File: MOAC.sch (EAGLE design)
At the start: 57 parts, among them IC1 ATMEGA32U4-QFN

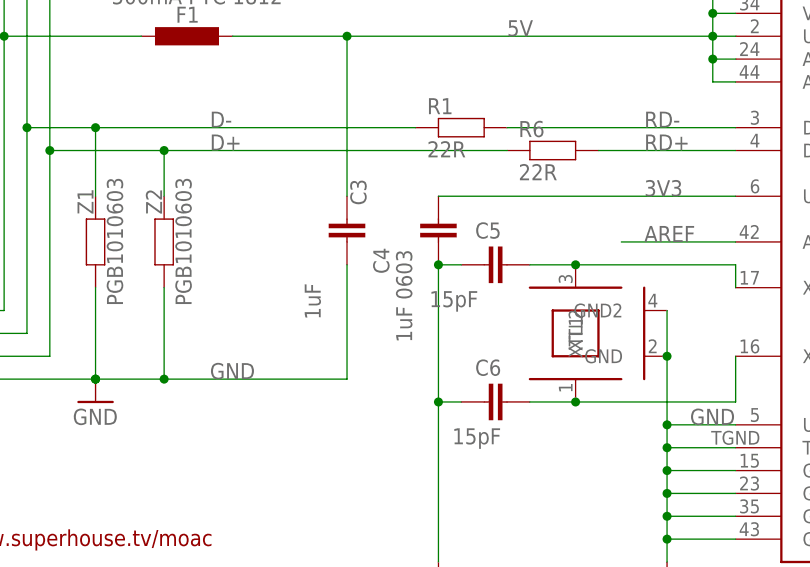
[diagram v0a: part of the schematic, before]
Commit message: Improved designators
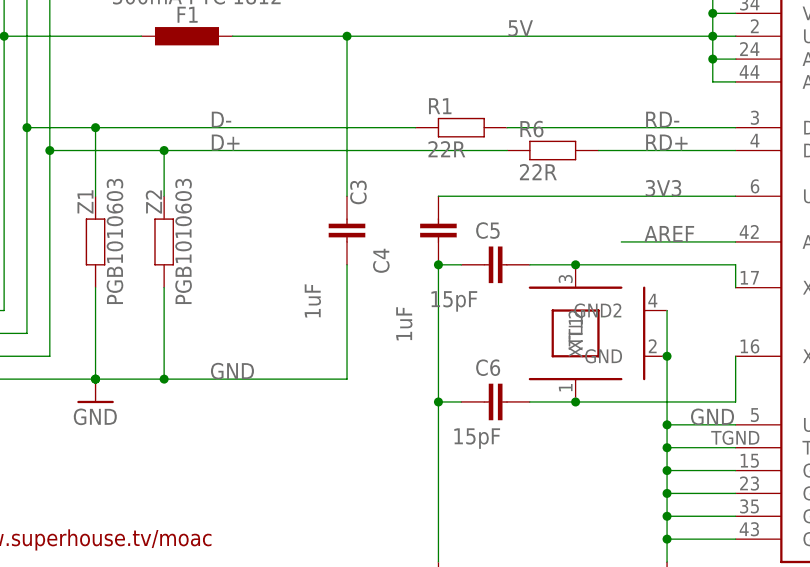
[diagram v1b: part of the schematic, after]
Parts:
- C4: value 1uF 0603 -> 1uF
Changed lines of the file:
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@@
 <part name="C6" library="freetronics-master-v1.1" deviceset="CAP" device="0603" value="15pF"/>
 <part name="GND16" library="SparkFun" deviceset="GND" device=""/>
-<part name="C4" library="freetronics-master-v1.1" deviceset="CAP" device="0603" value="1uF 0603"/>
+<part name="C4" library="freetronics-master-v1.1" deviceset="CAP" device="0603" value="1uF"/>
 <part name="GND5" library="SparkFun" deviceset="GND" device=""/>
 <part name="XTL1" library="freetronics-jon" deviceset="CRYSTAL-GND" device="3X2" value="16MHz"/>

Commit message: Replaced parts using SuperHouse libraries to add 3D models
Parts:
- removed JP2: OLED, freetronics-jon:M04PTH
- removed S1, S2, S3, S4, S5, S6, S7, S8: 3.5mm, freetronics-jon:AUDIO-JACK-PJ321
- removed S21: RESET, freetronics-jon:TAC_SWITCH_2PINSMT
- removed S22: HWB, freetronics-jon:TAC_SWITCH_2PINSMT
- removed U$15: USB-C, freetronics-jon:USB-C
- added J1, J2, J3, J4, J5, J6, J7, J8: 3.5mm, SuperHouse-Connectors:AUDIO-JACK-PJ321
- added J9: USB-C, SuperHouse-Connectors:USB-C
- added MOD1: OLED-I2C128X32-0.91, SuperHouse-Displays:OLED-I2C128X32-0.91
- added S10: HWB, SuperHouse-Switches:TAC_SWITCH_2PINSMT
- added S9: RESET, SuperHouse-Switches:TAC_SWITCH_2PINSMT
- C1, C2, C3, C4, C5, C6: device freetronics-master-v1.1:CAP0603 -> SuperHouse-DiscreteSemi:CAP0603
- F1: device rcl:L-EUL1812 -> SuperHouse-Fuses:PTC050
- ICSP: device pinhead:PINHD-2X3 -> SuperHouse-Connectors:ICSPPTH
- JP1: device freetronics-jon:M02PTH -> SuperHouse-Connectors:M02-PLAIN
- LED1, LED2, LED3, LED4: device freetronics-jon:LED0603 -> SuperHouse-LEDs:LED0603
- PIEZO: device freetronics-master-v1:BUZZERSMD12X12 -> SuperHouse-Audio:BUZZERSMD12X12
- R1, R10, R11, R12, R13, R14, R15, R16, R17, R19, R20, R21, R22, R23, R24, R25, R3, R4, R5, R6, R8, R9: device freetronics-jon:RESISTOR0603 -> SuperHouse-DiscreteSemi:RESISTOR0603
- R18, R7: device freetronics-original:RESISTOR0603 -> SuperHouse-DiscreteSemi:RESISTOR0603
- R2: device freetronics-master-v1.1:RESISTOR0603 -> SuperHouse-DiscreteSemi:RESISTOR0603
- XTL1: device freetronics-jon:CRYSTAL-GND3X2 -> SuperHouse-Oscillators:CRYSTAL-GND3X2
- Z1, Z2: device freetronics-master-v1.1:RESISTOR0603 -> SuperHouse-DiscreteSemi:TVS0603
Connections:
- net 5V: now also MOD1.VCC; no longer JP2.3
- net D+: now also J9.D+@A6, J9.D+@B6; no longer U$15.D+@A6, U$15.D+@B6
- net D-: now also J9.D-@A7, J9.D-@B7; no longer U$15.D-@A7, U$15.D-@B7
- net D2_SDA: now also MOD1.SDA; no longer JP2.1
- net D3_SCL: now also MOD1.SCL; no longer JP2.2
- net GND: now also J1.3, J2.3, J3.3, J4.3, J5.3, J6.3, J7.3, J8.3, J9.GND@A1, J9.GND@A12, J9.GND@B1, J9.GND@B12, J9.GND@CASE1, J9.GND@CASE2, J9.GND@CASE3, J9.GND@CASE4, J9.GND@FIX1, J9.GND@FIX2, J9.GND@FIX3, J9.GND@FIX4, MOD1.GND, S10.S, S9.P; no longer JP2.4, S1.3, S2.3, S21.P, S22.S, S3.3, S4.3, S5.3, S6.3, S7.3, S8.3, U$15.GND@A1, U$15.GND@A12, U$15.GND@B1, U$15.GND@B12, U$15.GND@CASE1, U$15.GND@CASE2, U$15.GND@CASE3, U$15.GND@CASE4, U$15.GND@FIX1, U$15.GND@FIX2, U$15.GND@FIX3, U$15.GND@FIX4
- net HWB: now also S10.P; no longer S22.P
- net N$1: now also J9.CC2; no longer U$15.CC2
- net N$10: now also J5.4A, J5.4B; no longer S5.4A, S5.4B
- net N$13: now also J6.4A, J6.4B; no longer S6.4A, S6.4B
- net N$14: now also J7.4A, J7.4B; no longer S7.4A, S7.4B
- net N$15: now also J8.4A, J8.4B; no longer S8.4A, S8.4B
- net N$3: now also J1.4A, J1.4B; no longer S1.4A, S1.4B
- net N$4: now also J2.4A, J2.4B; no longer S2.4A, S2.4B
- net N$5: now also J3.4A, J3.4B; no longer S3.4A, S3.4B
- net N$67: now also J9.CC1; no longer U$15.CC1
- net N$9: now also J4.4A, J4.4B; no longer S4.4A, S4.4B
- net RESET: now also S9.S; no longer S21.S
- net USB+: now also J9.V+@A4, J9.V+@A9, J9.V+@B4, J9.V+@B9; no longer U$15.V+@A4, U$15.V+@A9, U$15.V+@B4, U$15.V+@B9
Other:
- note added: "(C)2019 SuperHouse Automation Pty Ltd: www.superhouse.tv"
- note added: "V1.1 (2019-07-07)"
- note removed: "(C)2018 SuperHouse Automation Pty Ltd: www.superhouse.tv"
- note removed: "V1.0 (2018-10-10)"

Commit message: Replaced 128x32 OLED with 128x64, 1.3in for v2.0 release
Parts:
- removed MOD1: OLED-I2C128X32-0.91, SuperHouse-Displays:OLED-I2C128X32-0.91
- added MOD2: OLED-I2C128X64-1.3-HO, SuperHouse-Displays:OLED-I2C128X64-1.3-HO
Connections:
- net 5V: now also MOD2.VCC; no longer MOD1.VCC
- net D2_SDA: now also MOD2.SDA; no longer MOD1.SDA
- net D3_SCL: now also MOD2.SCL; no longer MOD1.SCL
- net GND: now also MOD2.GND; no longer MOD1.GND
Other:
- note added: "(C)2018-2019 SuperHouse Automation Pty Ltd: www.superhouse.tv"
- note added: "128x64 OLED Module"
- note added: "V2.0 (2019-07-11)"
- note removed: "(C)2019 SuperHouse Automation Pty Ltd: www.superhouse.tv"
- note removed: "128x32 OLED Header"
- note removed: "V1.1 (2019-07-07)"
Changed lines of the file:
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@@
 <part name="U$16" library="SparkFun" deviceset="5V" device=""/>
 <part name="JP1" library="SuperHouse-Connectors" library_urn="urn:adsk.eagle:library:11765989" deviceset="M02" device="-PLAIN" package3d_urn="urn:adsk.eagle:package:11818419/1" value="5V"/>
-<part name="MOD1" library="SuperHouse-Displays" library_urn="urn:adsk.eagle:library:11966779" deviceset="OLED-I2C" device="128X32-0.91" package3d_urn="urn:adsk.eagle:package:11973684/2"/>
+<part name="MOD2" library="SuperHouse-Displays" library_urn="urn:adsk.eagle:library:11966779" deviceset="OLED-I2C" device="128X64-1.3-HO" package3d_urn="urn:adsk.eagle:package:12058301/2" value="OLED-I2C128X64-1.3-HO"/>
 </parts>
 <sheets>
@@
 bootloader with the jumper.</text>
 <text x="7.62" y="20.32" size="3.048" layer="94">Mini Open Adaptive Controller</text>
-<text x="38.1" y="14.478" size="1.778" layer="94">V1.1 (2019-07-07)</text>
+<text x="38.1" y="14.478" size="1.778" layer="94">V2.0 (2019-07-11)</text>
 <text x="7.62" y="14.478" size="1.778" layer="94">SKU: MOAC</text>
-<text x="7.366" y="9.398" size="1.778" layer="94">(C)2019 SuperHouse Automation Pty Ltd: www.superhouse.tv</text>
+<text x="7.366" y="9.398" size="1.778" layer="94">(C)2018-2019 SuperHouse Automation Pty Ltd: www.superhouse.tv</text>
 <text x="7.366" y="6.35" size="1.778" layer="94">Licensed under the TAPR Open Hardware License: www.tapr.org/ohl</text>
 <text x="68.326" y="14.478" size="1.778" layer="94">www.superhouse.tv/moac</text>
@@
 <wire x1="109.22" y1="124.46" x2="109.22" y2="101.6" width="0.4064" layer="97" style="longdash"/>
 <text x="218.44" y="81.28" size="1.778" layer="97">Button3</text>
-<text x="111.76" y="149.86" size="2.54" layer="94" ratio="12">128x32 OLED Header</text>
+<text x="111.76" y="149.86" size="2.54" layer="94" ratio="12">128x64 OLED Module</text>
 <wire x1="109.22" y1="154.94" x2="154.94" y2="154.94" width="0.4064" layer="97" style="longdash"/>
 <wire x1="109.22" y1="124.46" x2="154.94" y2="124.46" width="0.4064" layer="97" style="longdash"/>
@@
 <attribute name="NAME" x="193.04" y="151.638" size="1.778" layer="95" rot="R180"/>
 </instance>
-<instance part="MOD1" gate="G$1" x="134.62" y="137.16" smashed="yes">
-<attribute name="NAME" x="129.54" y="142.748" size="1.778" layer="95"/>
+<instance part="MOD2" gate="G$1" x="132.08" y="137.16" smashed="yes">
+<attribute name="NAME" x="127" y="142.748" size="1.778" layer="95"/>
 <attribute name="VALUE" x="119.38" y="129.54" size="1.778" layer="96"/>
 </instance>
@@
 </segment>
 <segment>
-<pinref part="MOD1" gate="G$1" pin="VCC"/>
-<wire x1="144.78" y1="139.7" x2="149.86" y2="139.7" width="0.1524" layer="91"/>
+<wire x1="142.24" y1="139.7" x2="149.86" y2="139.7" width="0.1524" layer="91"/>
 <pinref part="U$2" gate="G$1" pin="5V"/>
 <wire x1="149.86" y1="139.7" x2="149.86" y2="142.24" width="0.1524" layer="91"/>
+<pinref part="MOD2" gate="G$1" pin="VCC"/>
 </segment>
 </net>
@@
 </segment>
 <segment>
-<pinref part="MOD1" gate="G$1" pin="GND"/>
 <pinref part="GND6" gate="1" pin="GND"/>
-<wire x1="144.78" y1="134.62" x2="149.86" y2="134.62" width="0.1524" layer="91"/>
+<wire x1="142.24" y1="134.62" x2="149.86" y2="134.62" width="0.1524" layer="91"/>
 <wire x1="149.86" y1="134.62" x2="149.86" y2="132.08" width="0.1524" layer="91"/>
+<pinref part="MOD2" gate="G$1" pin="GND"/>
 </segment>
 </net>
@@
 </segment>
 <segment>
-<wire x1="124.46" y1="139.7" x2="119.38" y2="139.7" width="0.1524" layer="91"/>
-<pinref part="MOD1" gate="G$1" pin="SDA"/>
+<wire x1="121.92" y1="139.7" x2="119.38" y2="139.7" width="0.1524" layer="91"/>
 <label x="119.38" y="139.7" size="1.27" layer="95" rot="R180" xref="yes"/>
+<pinref part="MOD2" gate="G$1" pin="SDA"/>
 </segment>
 </net>
@@
 </segment>
 <segment>
-<wire x1="124.46" y1="134.62" x2="119.38" y2="134.62" width="0.1524" layer="91"/>
-<pinref part="MOD1" gate="G$1" pin="SCL"/>
+<wire x1="121.92" y1="134.62" x2="119.38" y2="134.62" width="0.1524" layer="91"/>
 <label x="119.38" y="134.62" size="1.27" layer="95" rot="R180" xref="yes"/>
-</segment>
-</net>
+<pinref part="MOD2" gate="G$1" pin="SCL"/>
+</segment>
+</net>

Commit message: Changed ATmega32U4 from QFN to TQFP to save Jon's sanity for v2.0 release
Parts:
- removed JP1: 5V, SuperHouse-Connectors:M02-PLAIN
- IC1: value ATMEGA32U4-QFN -> ATMEGA32U4NT-TQFP; device freetronics-jon:ATMEGA32U4-QFN -> SuperHouse-MCUs:ATMEGA32U4NT-TQFP
- SJ1: device freetronics-jon:SJN -> SuperHouse-Jumpers:SJ-NORMAL
- SJ2: device freetronics-jon:SJCN -> SuperHouse-Jumpers:SJC-NORMAL
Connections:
- net 5V: no longer JP1.1
- net GND: no longer IC1.TGND, JP1.2

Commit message: Changed button 8 from A11 to A7, to fix Jon's silly mistake from way back in v1.0
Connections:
- net D10_A11 renamed D10_A10
- net D8_A9 renamed D8_A8
- net D9_A10 renamed D9_A9
- removed net D12_A7: IC1.PD6(T1/OC4D/ADC9), R21.2, R25.1
- removed net D6_A8: IC1.PD7(OC4D/ADC10/T0)
- new net D12_A11: IC1.PD6(T1/OC4D/ADC9)
- new net D6_A7: IC1.PD7(OC4D/ADC10/T0), R21.2, R25.1
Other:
- note added: "V2.1 (2019-07-31)"
- note removed: "V2.0 (2019-07-11)"
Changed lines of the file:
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@@
 <part name="U$16" library="SuperHouse-SupplySymbols" library_urn="urn:adsk.eagle:library:11790503" deviceset="5V" device=""/>
 <part name="MOD2" library="SuperHouse-Displays" library_urn="urn:adsk.eagle:library:11966779" deviceset="OLED-I2C" device="128X64-1.3-HO" package3d_urn="urn:adsk.eagle:package:12058301/2" value="OLED-I2C128X64-1.3-HO"/>
-<part name="IC1" library="SuperHouse-MCUs" library_urn="urn:adsk.eagle:library:11815114" deviceset="ATMEGA32U4NT" device="-TQFP" package3d_urn="urn:adsk.eagle:package:12190647/2"/>
+<part name="IC1" library="SuperHouse-MCUs" library_urn="urn:adsk.eagle:library:11815114" deviceset="ATMEGA32U4NT" device="-TQFP" package3d_urn="urn:adsk.eagle:package:12190647/3"/>
 </parts>
 <sheets>
@@
 bootloader with the jumper.</text>
 <text x="7.62" y="20.32" size="3.048" layer="94">Mini Open Adaptive Controller</text>
-<text x="38.1" y="14.478" size="1.778" layer="94">V2.0 (2019-07-11)</text>
+<text x="38.1" y="14.478" size="1.778" layer="94">V2.1 (2019-07-31)</text>
 <text x="7.62" y="14.478" size="1.778" layer="94">SKU: MOAC</text>
 <text x="7.366" y="9.398" size="1.778" layer="94">(C)2018-2019 SuperHouse Automation Pty Ltd: www.superhouse.tv</text>
@@
 <text x="218.44" y="76.2" size="1.778" layer="97">Button1</text>
 <text x="218.44" y="78.74" size="1.778" layer="97">Button2</text>
-<text x="218.44" y="30.48" size="1.778" layer="97">Button8</text>
+<text x="218.44" y="33.02" size="1.778" layer="97">Button8</text>
 <text x="218.44" y="25.4" size="1.778" layer="97">Button7</text>
 <text x="218.44" y="88.9" size="1.778" layer="97">Button6</text>
@@
 </segment>
 </net>
-<net name="D6_A8" class="0">
-<segment>
-<wire x1="203.2" y1="33.02" x2="215.9" y2="33.02" width="0.1524" layer="91"/>
+<net name="D6_A7" class="0">
+<segment>
+<wire x1="203.2" y1="33.02" x2="228.6" y2="33.02" width="0.1524" layer="91"/>
 <label x="205.74" y="33.02" size="1.778" layer="95"/>
 <pinref part="IC1" gate="G$1" pin="PD7(OC4D/ADC10/T0)"/>
-</segment>
-</net>
-<net name="D12_A7" class="0">
-<segment>
-<wire x1="203.2" y1="30.48" x2="228.6" y2="30.48" width="0.1524" layer="91"/>
-<label x="205.74" y="30.48" size="1.778" layer="95"/>
-<pinref part="IC1" gate="G$1" pin="PD6(T1/OC4D/ADC9)"/>
 </segment>
 <segment>
@@
 </segment>
 </net>
-<net name="D8_A9" class="0">
+<net name="D8_A8" class="0">
 <segment>
 <wire x1="203.2" y1="48.26" x2="215.9" y2="48.26" width="0.1524" layer="91"/>
@@
 </segment>
 </net>
-<net name="D9_A10" class="0">
+<net name="D9_A9" class="0">
 <segment>
 <wire x1="203.2" y1="50.8" x2="215.9" y2="50.8" width="0.1524" layer="91"/>
@@
 </segment>
 </net>
-<net name="D10_A11" class="0">
+<net name="D10_A10" class="0">
 <segment>
 <wire x1="203.2" y1="53.34" x2="215.9" y2="53.34" width="0.1524" layer="91"/>
@@
 </segment>
 </net>
+<net name="D12_A11" class="0">
+<segment>
+<wire x1="203.2" y1="30.48" x2="215.9" y2="30.48" width="0.1524" layer="91"/>
+<label x="205.74" y="30.48" size="1.778" layer="95"/>
+<pinref part="IC1" gate="G$1" pin="PD6(T1/OC4D/ADC9)"/>
+</segment>
+</net>

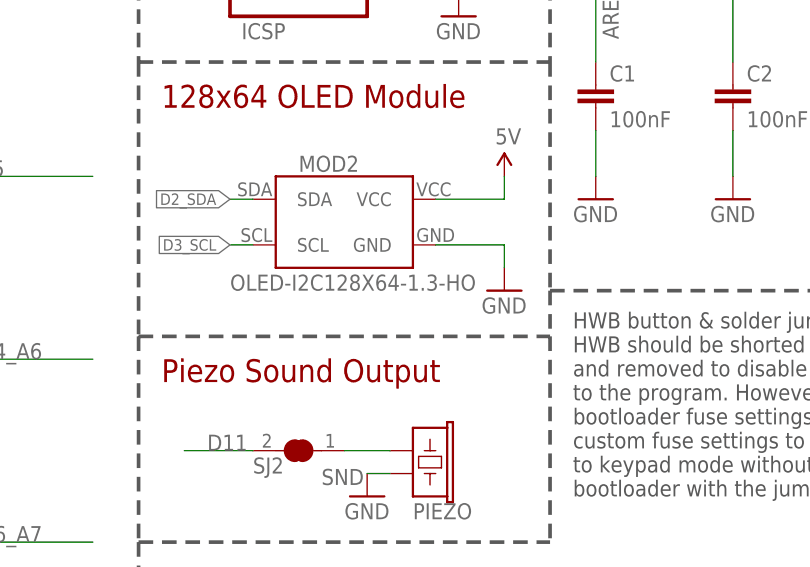
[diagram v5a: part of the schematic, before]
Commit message: Changed display from 128x32 to 128x64
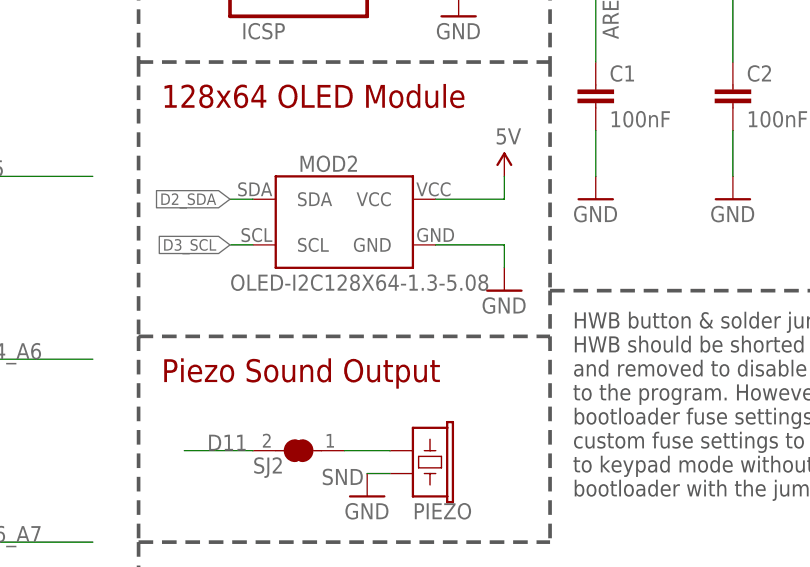
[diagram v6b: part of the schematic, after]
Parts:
- MOD2: value OLED-I2C128X64-1.3-HO -> OLED-I2C128X64-1.3-5.08; device SuperHouse-Displays:OLED-I2C128X64-1.3-HO -> SuperHouse-Displays:OLED-I2C128X64-1.3-5.08
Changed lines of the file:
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@@
 <?xml version="1.0" encoding="utf-8"?>
 <!DOCTYPE eagle SYSTEM "eagle.dtd">
-<eagle version="9.4.2">
+<eagle version="9.5.2">
 <drawing>
 <settings>
@@
 <part name="R13" library="SuperHouse-DiscreteSemi" library_urn="urn:adsk.eagle:library:11768461" deviceset="RESISTOR" device="0603" package3d_urn="urn:adsk.eagle:package:11768543/2" value="10K"/>
 <part name="U$16" library="SuperHouse-SupplySymbols" library_urn="urn:adsk.eagle:library:11790503" deviceset="5V" device=""/>
-<part name="MOD2" library="SuperHouse-Displays" library_urn="urn:adsk.eagle:library:11966779" deviceset="OLED-I2C" device="128X64-1.3-HO" package3d_urn="urn:adsk.eagle:package:12058301/2" value="OLED-I2C128X64-1.3-HO"/>
+<part name="MOD2" library="SuperHouse-Displays" library_urn="urn:adsk.eagle:library:11966779" deviceset="OLED-I2C" device="128X64-1.3-5.08" package3d_urn="urn:adsk.eagle:package:16152188/2" value="OLED-I2C128X64-1.3-5.08"/>
 <part name="IC1" library="SuperHouse-MCUs" library_urn="urn:adsk.eagle:library:11815114" deviceset="ATMEGA32U4NT" device="-TQFP" package3d_urn="urn:adsk.eagle:package:12190647/3"/>
 </parts>
